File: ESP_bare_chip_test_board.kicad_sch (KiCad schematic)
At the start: 0 parts

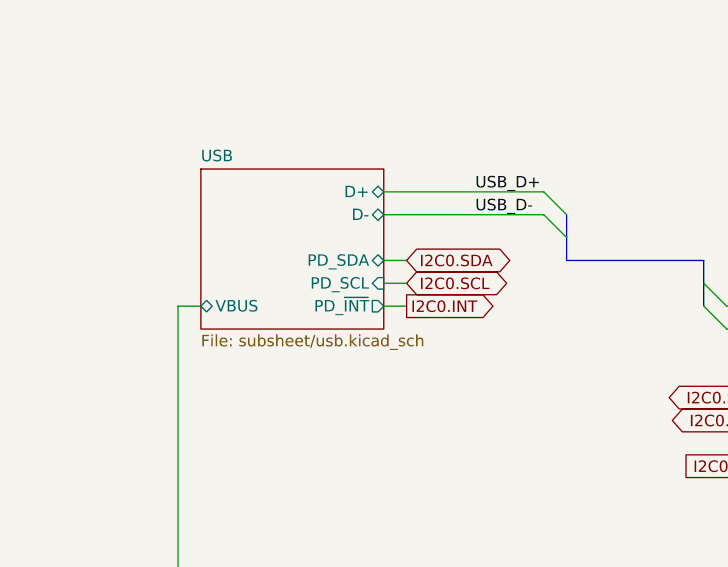
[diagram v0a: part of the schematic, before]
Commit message: Removed USB-PD circuit - simplifies board
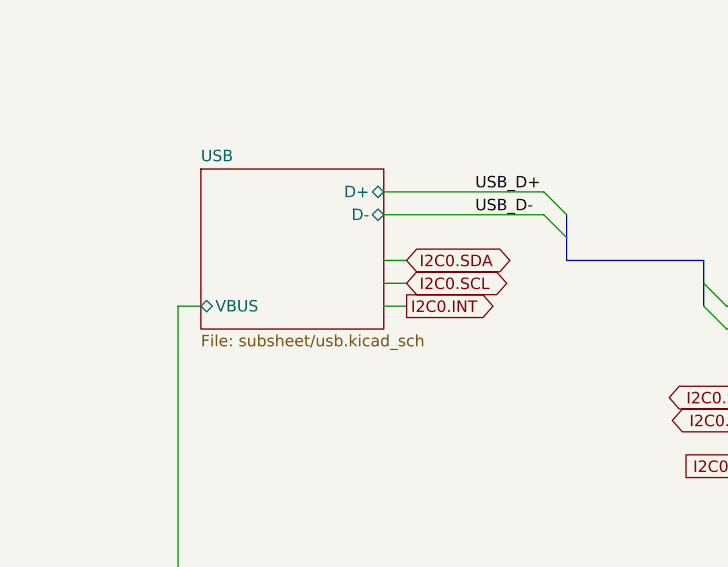
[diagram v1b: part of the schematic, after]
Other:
- sheet USB ports: added none; removed PD_SCL, PD_SDA, PD_~{INT}
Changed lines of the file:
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@@
-			)
-		)
-		(pin "PD_~{INT}" output
-			(at 38.1 33.02 0)
-			(effects
-				(font
-					(size 1.27 1.27)
-				)
-				(justify right)
-			)
-		)
-		(pin "PD_SDA" bidirectional
-			(at 38.1 27.94 0)
-			(effects
-				(font
-					(size 1.27 1.27)
-				)
-				(justify right)
 			)
 		)
@@
 			)
 		)
-		(pin "PD_SCL" input
-			(at 38.1 30.48 0)
-			(effects
-				(font
-					(size 1.27 1.27)
-				)
-				(justify right)
-			)
-		)

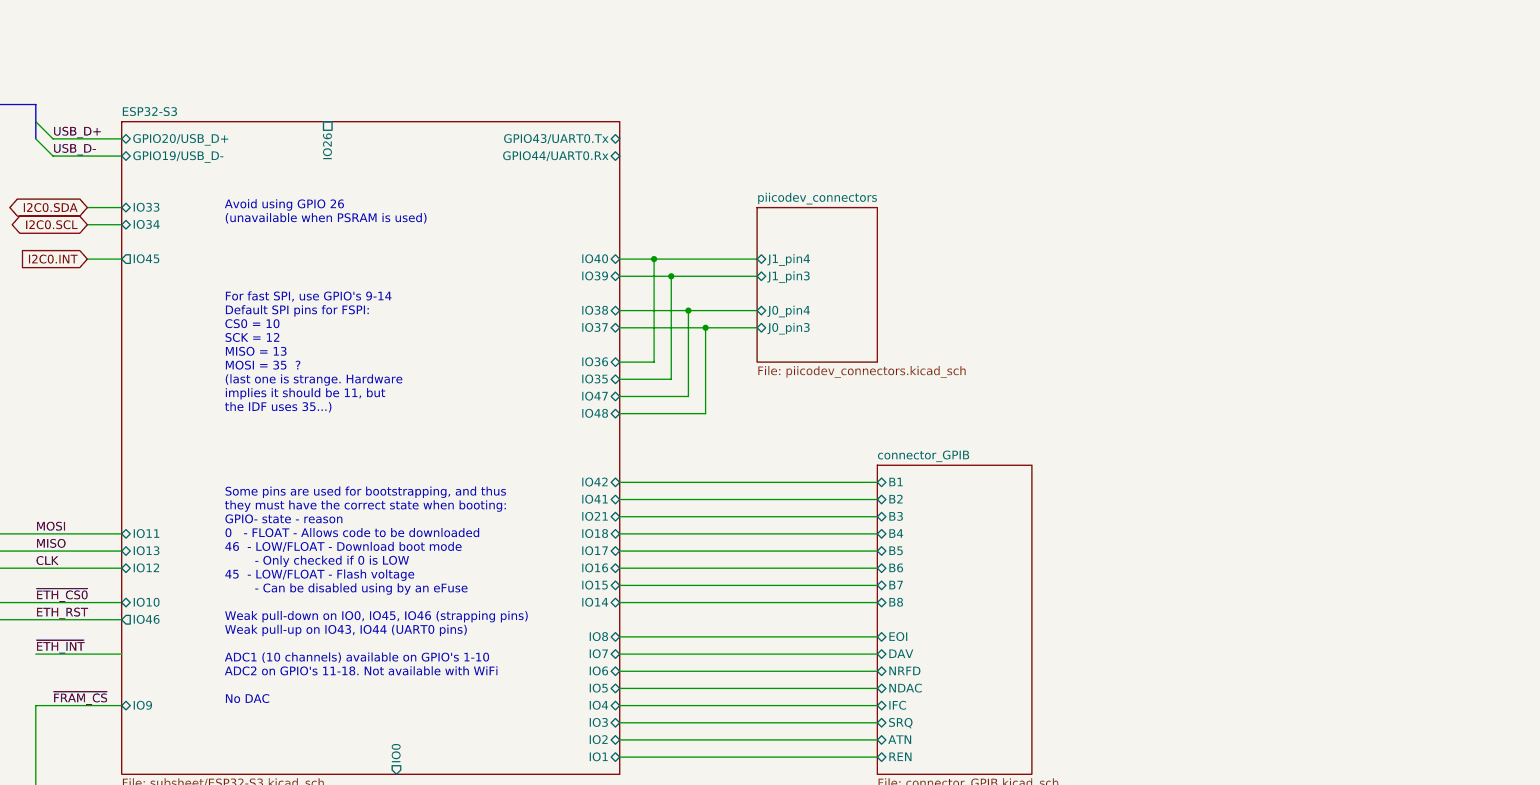
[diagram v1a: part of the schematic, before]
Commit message: Started wiring up traces
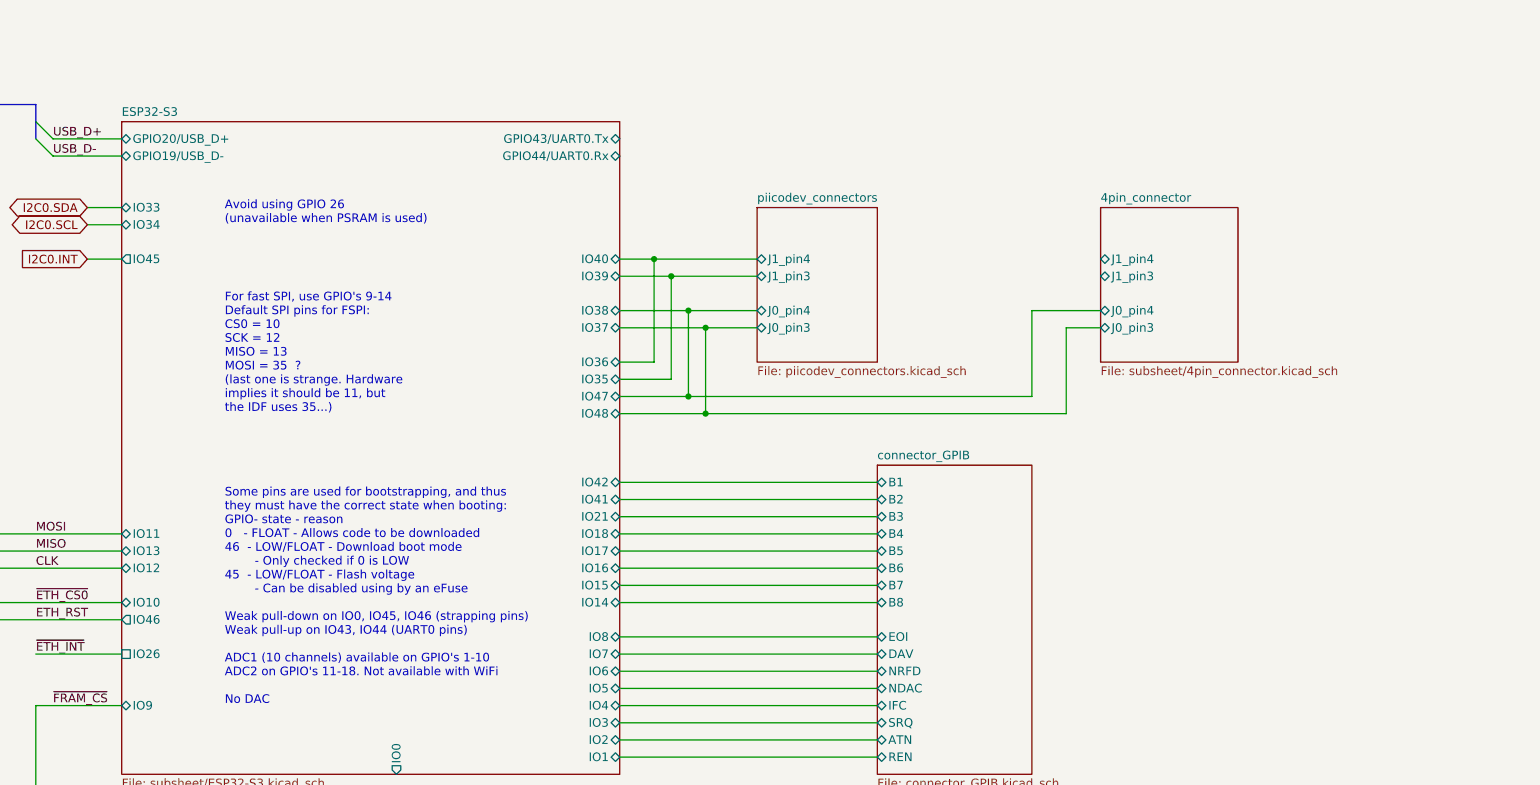
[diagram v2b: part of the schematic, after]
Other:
- added sheet 4pin_connector (subsheet/4pin_connector.kicad_sch)
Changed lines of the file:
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@@
+	)
+	(junction
+		(at 172.72 73.66)
+		(diameter 0)
+		(color 0 0 0 0)
 	)
 	(junction
@@
 	)
 	(junction
+		(at 170.18 71.12)
+		(diameter 0)
+		(color 0 0 0 0)
+	)
+	(junction
 		(at 66.04 91.44)
 		(diameter 0)
@@
 	(wire
 		(pts
+			(xy 170.18 71.12) (xy 220.98 71.12)
+		)
+		(stroke
+			(width 0)
+			(type default)
+		)
+	)
+	(wire
+		(pts
 			(xy 160.02 50.8) (xy 165.1 50.8)
 		)
@@
 	(wire
 		(pts
+			(xy 226.06 60.96) (xy 231.14 60.96)
+		)
+		(stroke
+			(width 0)
+			(type default)
+		)
+	)
+	(wire
+		(pts
 			(xy 45.72 124.46) (xy 64.77 124.46)
 		)
@@
 	(wire
 		(pts
+			(xy 172.72 73.66) (xy 226.06 73.66)
+		)
+		(stroke
+			(width 0)
+			(type default)
+		)
+	)
+	(wire
+		(pts
 			(xy 160.02 93.98) (xy 198.12 93.98)
 		)
@@
 	(wire
 		(pts
+			(xy 220.98 58.42) (xy 231.14 58.42)
+		)
+		(stroke
+			(width 0)
+			(type default)
+		)
+	)
+	(wire
+		(pts
 			(xy 45.72 96.52) (xy 63.5 96.52)
 		)
@@
 	(wire
 		(pts
+			(xy 226.06 73.66) (xy 226.06 60.96)
+		)
+		(stroke
+			(width 0)
+			(type default)
+		)
+	)
+	(wire
+		(pts
 			(xy 76.2 35.56) (xy 86.36 35.56)
 		)
@@
 		(pts
 			(xy 160.02 73.66) (xy 172.72 73.66)
+		)
+		(stroke
+			(width 0)
+			(type default)
+		)
+	)
+	(wire
+		(pts
+			(xy 220.98 71.12) (xy 220.98 58.42)
 		)
 		(stroke
@@
 		)
 		(pin "IO26" passive
-			(at 116.84 30.48 90)
-			(effects
-				(font
-					(size 1.27 1.27)
-				)
-				(justify right)
+			(at 86.36 109.22 180)
+			(effects
+				(font
+					(size 1.27 1.27)
+				)
+				(justify left)
 			)
 		)
@@
 			)
 		)
+		(instances
+			(project "ESP_bare_chip_test_board"
+				(path "/45b6f84a-e69b-48be-a49b-bc68872e2c15"
+					(page "13")
+				)
+			)
+		)
+	)
+	(sheet
+		(at 231.14 43.18)
+		(size 20.32 22.86)
+		(fields_autoplaced yes)
+		(stroke
+			(width 0.1524)
+			(type solid)
+		)
+		(fill
+			(color 255 229 191 1.0000)
+		)
+		(property "Sheetname" "4pin_connector"
+			(at 231.14 42.4684 0)
+			(effects
+				(font
+					(size 1.27 1.27)
+				)
+				(justify left bottom)
+			)
+		)
+		(property "Sheetfile" "subsheet/4pin_connector.kicad_sch"
+			(at 231.14 66.6246 0)
+			(effects
+				(font
+					(size 1.27 1.27)
+				)
+				(justify left top)
+			)
+		)
+		(pin "J0_pin3" bidirectional
+			(at 231.14 60.96 180)
+			(effects
+				(font
+					(size 1.27 1.27)
+				)
+				(justify left)
+			)
+		)
+		(pin "J0_pin4" bidirectional
+			(at 231.14 58.42 180)
+			(effects
+				(font
+					(size 1.27 1.27)
+				)
+				(justify left)
+			)
+		)
+		(pin "J1_pin3" bidirectional
+			(at 231.14 53.34 180)
+			(effects
+				(font
+					(size 1.27 1.27)
+				)
+				(justify left)
+			)
+		)
+		(pin "J1_pin4" bidirectional
+			(at 231.14 50.8 180)
+			(effects
+				(font
+					(size 1.27 1.27)
+				)
+				(justify left)
+			)
+		)

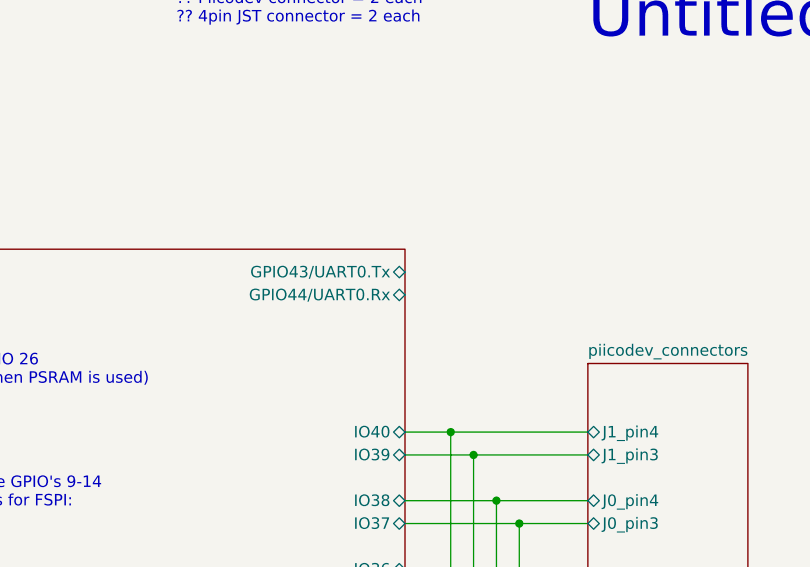
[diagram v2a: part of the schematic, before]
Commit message: More wiring - Ethernet, SPI flash
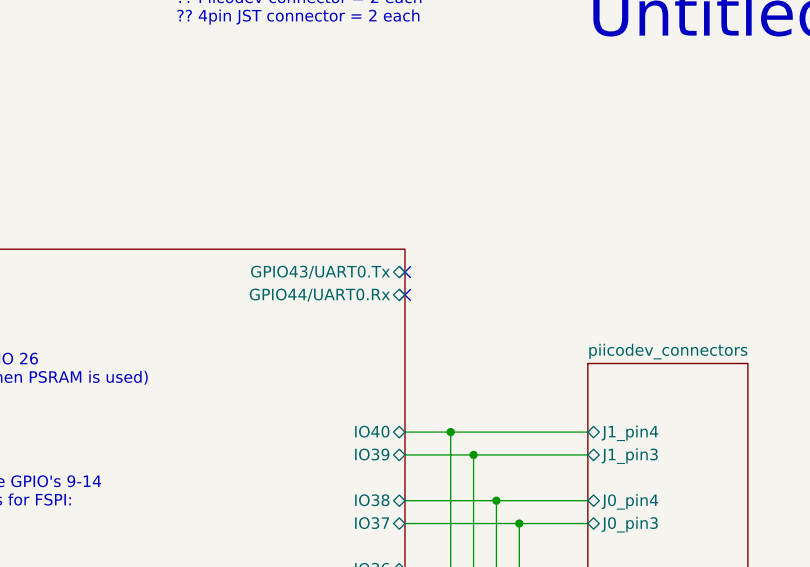
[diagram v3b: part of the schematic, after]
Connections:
- no-connect marks 0 -> 2
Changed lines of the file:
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@@
 		(color 0 0 0 0)
+	)
+	(no_connect
+		(at 160.02 35.56)
+	)
+	(no_connect
+		(at 160.02 33.02)
 	)
 	(bus_entry

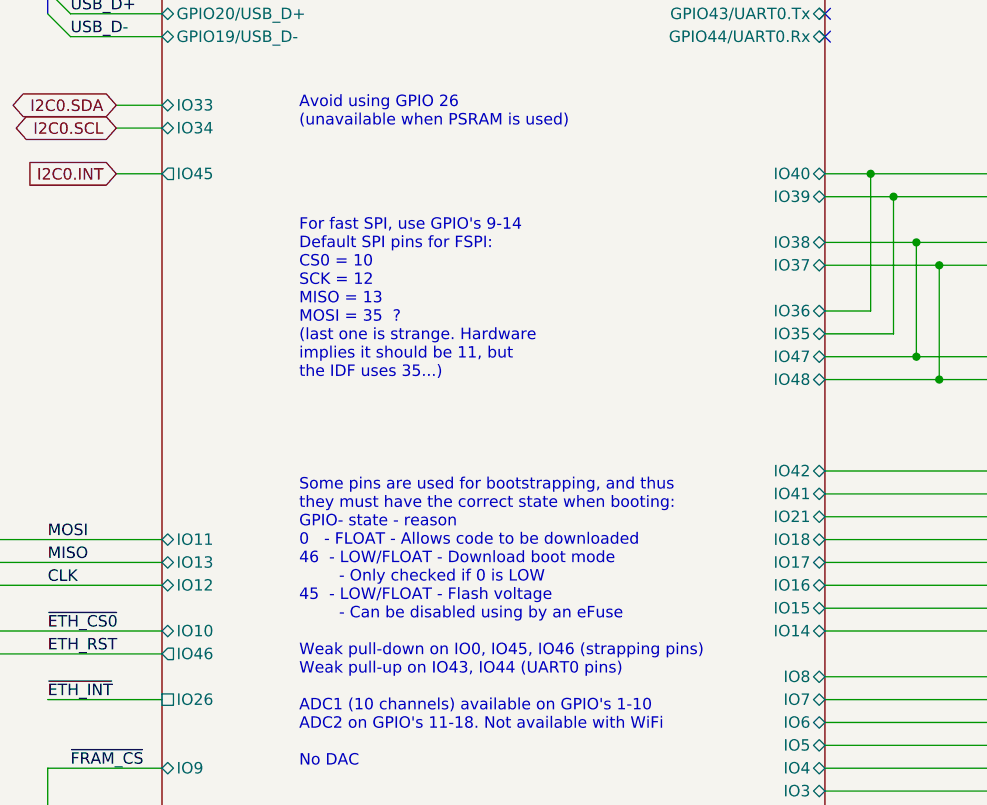
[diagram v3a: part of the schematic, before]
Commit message: More wiring - GPIB connector, partially routed
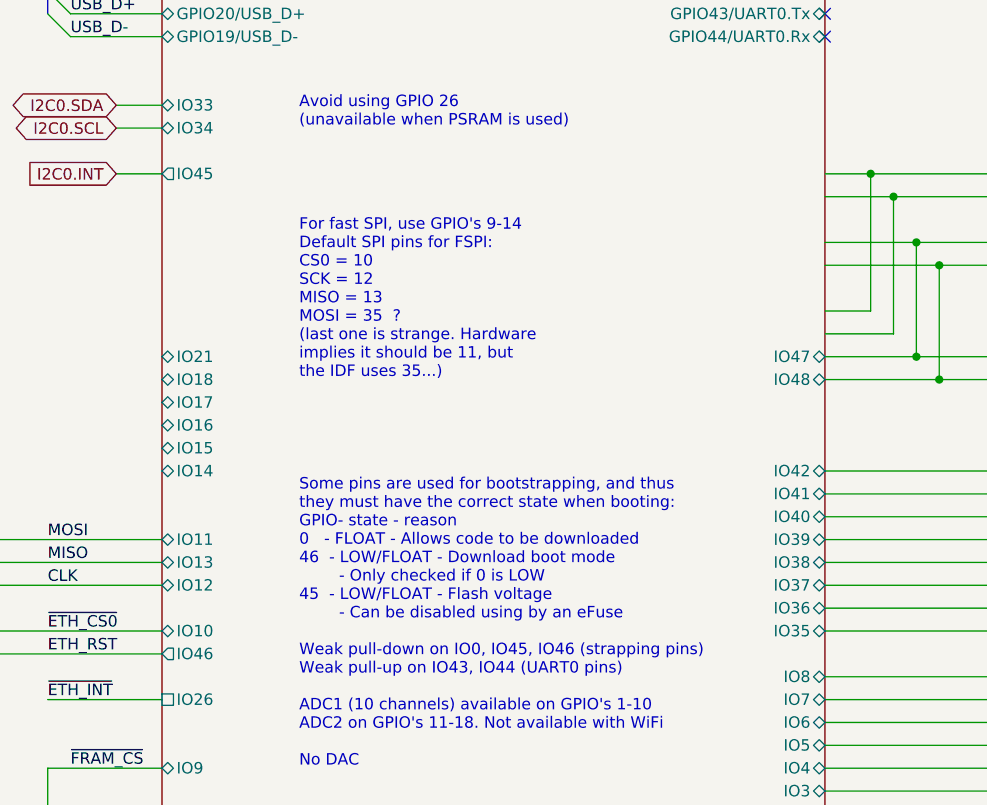
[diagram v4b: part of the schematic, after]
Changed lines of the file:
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@@
 		)
 		(pin "IO14" bidirectional
-			(at 160.02 101.6 0)
-			(effects
-				(font
-					(size 1.27 1.27)
-				)
-				(justify right)
+			(at 86.36 83.82 180)
+			(effects
+				(font
+					(size 1.27 1.27)
+				)
+				(justify left)
 			)
 		)
 		(pin "IO17" bidirectional
-			(at 160.02 93.98 0)
-			(effects
-				(font
-					(size 1.27 1.27)
-				)
-				(justify right)
+			(at 86.36 76.2 180)
+			(effects
+				(font
+					(size 1.27 1.27)
+				)
+				(justify left)
 			)
 		)
 		(pin "IO18" bidirectional
-			(at 160.02 91.44 0)
-			(effects
-				(font
-					(size 1.27 1.27)
-				)
-				(justify right)
+			(at 86.36 73.66 180)
+			(effects
+				(font
+					(size 1.27 1.27)
+				)
+				(justify left)
 			)
 		)
@@
 		)
 		(pin "IO21" bidirectional
-			(at 160.02 88.9 0)
-			(effects
-				(font
-					(size 1.27 1.27)
-				)
-				(justify right)
+			(at 86.36 71.12 180)
+			(effects
+				(font
+					(size 1.27 1.27)
+				)
+				(justify left)
 			)
 		)
 		(pin "IO38" bidirectional
-			(at 160.02 58.42 0)
+			(at 160.02 93.98 0)
 			(effects
 				(font
@@
 		)
 		(pin "IO15" bidirectional
-			(at 160.02 99.06 0)
-			(effects
-				(font
-					(size 1.27 1.27)
-				)
-				(justify right)
+			(at 86.36 81.28 180)
+			(effects
+				(font
+					(size 1.27 1.27)
+				)
+				(justify left)
 			)
 		)
 		(pin "IO16" bidirectional
+			(at 86.36 78.74 180)
+			(effects
+				(font
+					(size 1.27 1.27)
+				)
+				(justify left)
+			)
+		)
+		(pin "IO39" bidirectional
+			(at 160.02 91.44 0)
+			(effects
+				(font
+					(size 1.27 1.27)
+				)
+				(justify right)
+			)
+		)
+		(pin "IO37" bidirectional
 			(at 160.02 96.52 0)
-			(effects
-				(font
-					(size 1.27 1.27)
-				)
-				(justify right)
-			)
-		)
-		(pin "IO39" bidirectional
-			(at 160.02 53.34 0)
-			(effects
-				(font
-					(size 1.27 1.27)
-				)
-				(justify right)
-			)
-		)
-		(pin "IO37" bidirectional
-			(at 160.02 60.96 0)
 			(effects
 				(font
@@
 		)
 		(pin "IO35" bidirectional
-			(at 160.02 68.58 0)
+			(at 160.02 101.6 0)
 			(effects
 				(font
@@
 		)
 		(pin "IO36" bidirectional
-			(at 160.02 66.04 0)
+			(at 160.02 99.06 0)
 			(effects
 				(font
@@
 		)
 		(pin "IO40" bidirectional
-			(at 160.02 50.8 0)
-			(effects
-				(font
+			(at 160.02 88.9 0)
+			(effects
+				(font
